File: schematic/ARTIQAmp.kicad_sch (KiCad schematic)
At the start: 28 parts, among them J1 Power conneciton, J2 HD68, J3 HD68, J4 TSM-102-01-L-DV

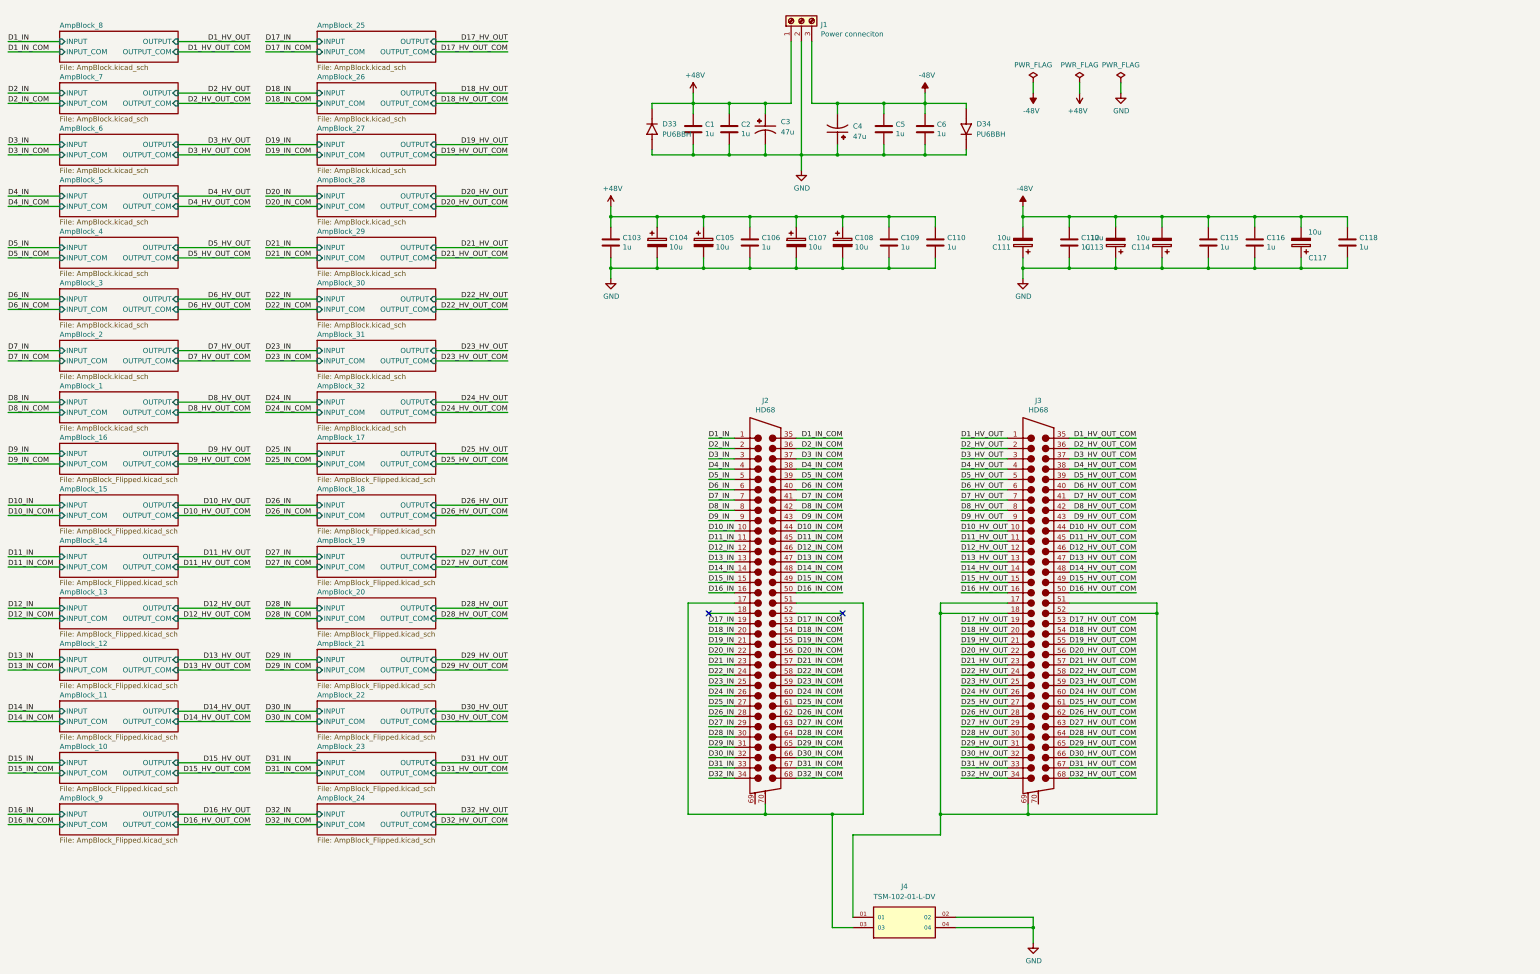
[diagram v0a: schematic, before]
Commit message: Update board design to better support enclosure with fan connect and diode connect headers. Also widen differential choke land pads and include enclosure CAD.
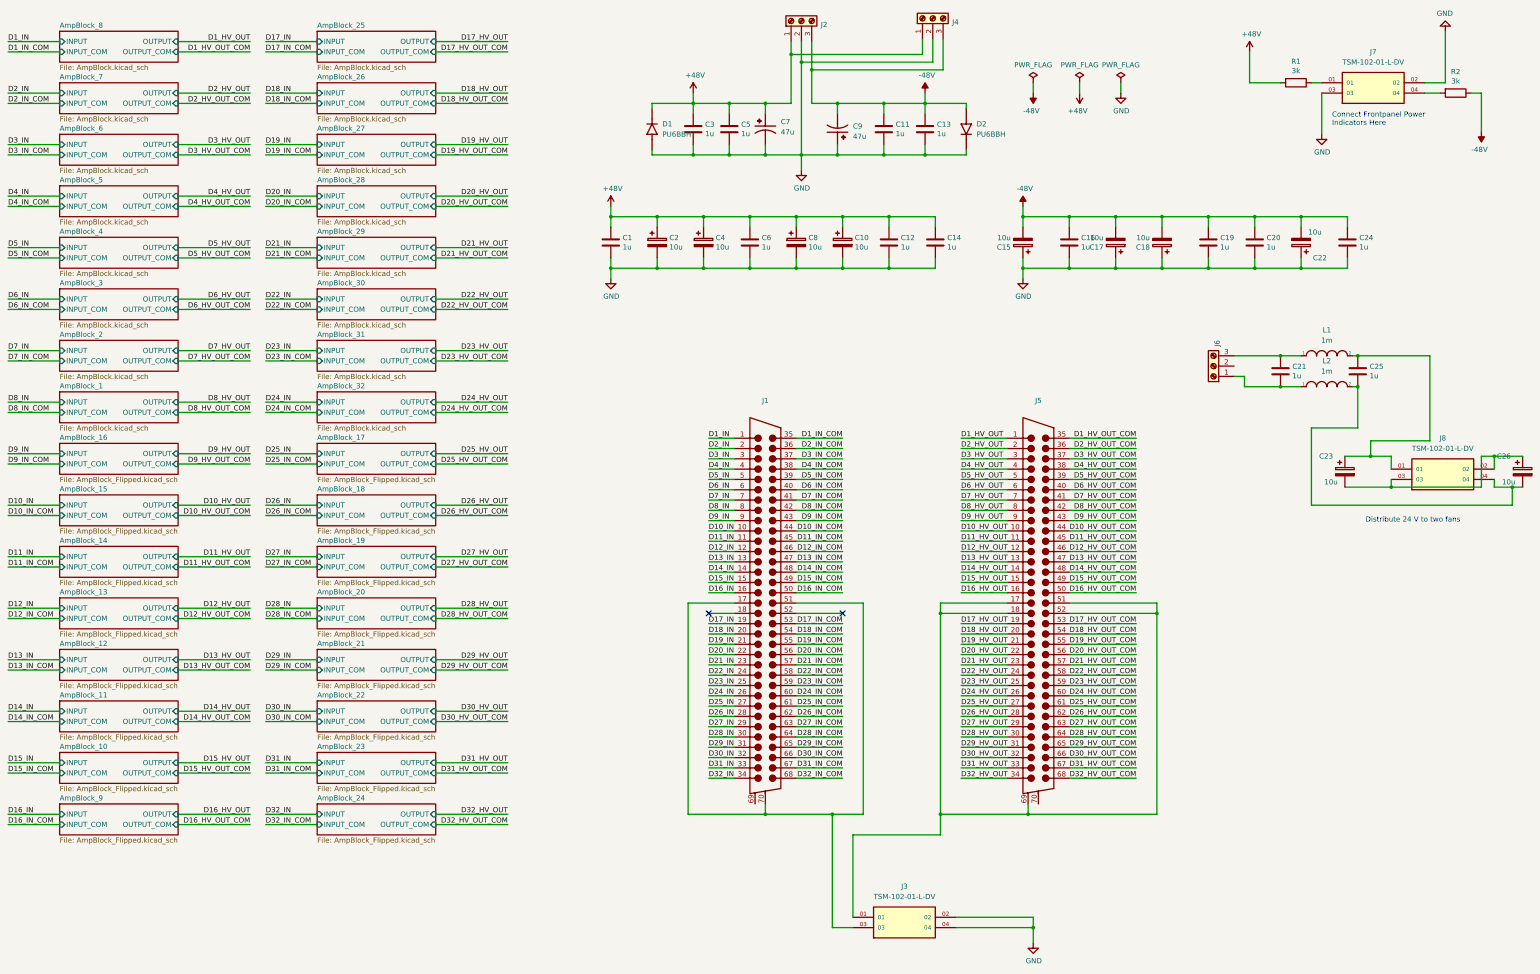
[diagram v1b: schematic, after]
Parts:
- added C21, C25: 1u, Capacitor_SMD:C_1206_3216Metric, symbol Device:C
- added C23, C26: 10u, ARTIQAmp:CAP_EEEFK1H100V, symbol Device:CP
- added J4, J6: (no value), TerminalBlock_Phoenix:TerminalBlock_Phoenix_PT-1,5-3-5.0-H_1x03_P5.00mm_Horizontal, symbol ARTIQAmp:Screw_Terminal_01x03
- added J7, J8: TSM-102-01-L-DV, SAMTEC_TSM-102-01-L-DV, symbol TSM-102-01-L-DV:TSM-102-01-L-DV
- added L1, L2: 1m, Inductor_SMD:L_1210_3225Metric, symbol pspice:INDUCTOR
- added R1, R2: 3k, Resistor_SMD:R_1206_3216Metric, symbol Device:R
- C1: renamed from C103; AVAILABILITY Y -> (none); Availability (none) -> Y; MANUFACTURER Samsung -> (none); MPN (none) -> CL31B105KCHNNNE; Manufacturer (none) -> Samsung; Manufacturer_Part_Number CL31B105KCHNNNE -> (none); Package (none) -> 1206
- C10: renamed from C108; AVAILABILITY Y -> (none); Availability (none) -> Y; MANUFACTURER United Chemi-Con -> (none); MPN (none) -> HHXD630ARA100MF80G; Manufacturer (none) -> United Chemi-Con; Manufacturer_Part_Number HHXD630ARA100MF80G -> (none); Package (none) -> Radial, Can - SMD
- C11: renamed from C5; AVAILABILITY Y -> (none); Availability (none) -> Y; MANUFACTURER Samsung -> (none); MPN (none) -> CL31B105KCHNNNE; Manufacturer (none) -> Samsung; Manufacturer_Part_Number CL31B105KCHNNNE -> (none); Package (none) -> 1206
- C12: renamed from C109; AVAILABILITY Y -> (none); Availability (none) -> Y; MANUFACTURER Samsung -> (none); MPN (none) -> CL31B105KCHNNNE; Manufacturer (none) -> Samsung; Manufacturer_Part_Number CL31B105KCHNNNE -> (none); Package (none) -> 1206
- C13: renamed from C6; AVAILABILITY Y -> (none); Availability (none) -> Y; MANUFACTURER Samsung -> (none); MPN (none) -> CL31B105KCHNNNE; Manufacturer (none) -> Samsung; Manufacturer_Part_Number CL31B105KCHNNNE -> (none); Package (none) -> 1206
- C14: renamed from C110; AVAILABILITY Y -> (none); Availability (none) -> Y; MANUFACTURER Samsung -> (none); MPN (none) -> CL31B105KCHNNNE; Manufacturer (none) -> Samsung; Manufacturer_Part_Number CL31B105KCHNNNE -> (none); Package (none) -> 1206
- C15: renamed from C111; AVAILABILITY Y -> (none); Availability (none) -> Y; MANUFACTURER United Chemi-Con -> (none); MPN (none) -> HHXD630ARA100MF80G; Manufacturer (none) -> United Chemi-Con; Manufacturer_Part_Number HHXD630ARA100MF80G -> (none); Package (none) -> Radial, Can - SMD; Type (none) -> SMT
- C16: renamed from C112; AVAILABILITY Y -> (none); Availability (none) -> Y; MANUFACTURER Samsung -> (none); MPN (none) -> CL31B105KCHNNNE; Manufacturer (none) -> Samsung; Manufacturer_Part_Number CL31B105KCHNNNE -> (none); Package (none) -> 1206
- C17: renamed from C113; AVAILABILITY Y -> (none); Availability (none) -> Y; MANUFACTURER United Chemi-Con -> (none); MPN (none) -> HHXD630ARA100MF80G; Manufacturer (none) -> United Chemi-Con; Manufacturer_Part_Number HHXD630ARA100MF80G -> (none); Package (none) -> Radial, Can - SMD
- C18: renamed from C114; AVAILABILITY Y -> (none); Availability (none) -> Y; MANUFACTURER United Chemi-Con -> (none); MPN (none) -> HHXD630ARA100MF80G; Manufacturer (none) -> United Chemi-Con; Manufacturer_Part_Number HHXD630ARA100MF80G -> (none); Package (none) -> Radial, Can - SMD
- C19: renamed from C115; AVAILABILITY Y -> (none); Availability (none) -> Y; MANUFACTURER Samsung -> (none); MPN (none) -> CL31B105KCHNNNE; Manufacturer (none) -> Samsung; Manufacturer_Part_Number CL31B105KCHNNNE -> (none); Package (none) -> 1206
- C2: renamed from C104; AVAILABILITY Y -> (none); Availability (none) -> Y; MANUFACTURER United Chemi-Con -> (none); MPN (none) -> HHXD630ARA100MF80G; Manufacturer (none) -> United Chemi-Con; Manufacturer_Part_Number HHXD630ARA100MF80G -> (none); Package (none) -> Radial, Can - SMD
- C20: renamed from C116; AVAILABILITY Y -> (none); Availability (none) -> Y; MANUFACTURER Samsung -> (none); MPN (none) -> CL31B105KCHNNNE; Manufacturer (none) -> Samsung; Manufacturer_Part_Number CL31B105KCHNNNE -> (none); Package (none) -> 1206
- C22: renamed from C117; AVAILABILITY Y -> (none); Availability (none) -> Y; MANUFACTURER United Chemi-Con -> (none); MPN (none) -> HHXD630ARA100MF80G; Manufacturer (none) -> United Chemi-Con; Manufacturer_Part_Number HHXD630ARA100MF80G -> (none); Package (none) -> Radial, Can - SMD
- C24: renamed from C118; AVAILABILITY Y -> (none); Availability (none) -> Y; MANUFACTURER Samsung -> (none); MPN (none) -> CL31B105KCHNNNE; Manufacturer (none) -> Samsung; Manufacturer_Part_Number CL31B105KCHNNNE -> (none); Package (none) -> 1206
- C3: renamed from C1; AVAILABILITY Y -> (none); Availability (none) -> Y; MANUFACTURER Samsung -> (none); MPN (none) -> CL31B105KCHNNNE; Manufacturer (none) -> Samsung; Manufacturer_Part_Number CL31B105KCHNNNE -> (none); Package (none) -> 1206
- C4: renamed from C105; AVAILABILITY Y -> (none); Availability (none) -> Y; MANUFACTURER United Chemi-Con -> (none); MPN (none) -> HHXD630ARA100MF80G; Manufacturer (none) -> United Chemi-Con; Manufacturer_Part_Number HHXD630ARA100MF80G -> (none); Package (none) -> Radial, Can - SMD
- C5: renamed from C2; AVAILABILITY Y -> (none); Availability (none) -> Y; MANUFACTURER Samsung -> (none); MPN (none) -> CL31B105KCHNNNE; Manufacturer (none) -> Samsung; Manufacturer_Part_Number CL31B105KCHNNNE -> (none); Package (none) -> 1206
- C6: renamed from C106; AVAILABILITY Y -> (none); Availability (none) -> Y; MANUFACTURER Samsung -> (none); MPN (none) -> CL31B105KCHNNNE; Manufacturer (none) -> Samsung; Manufacturer_Part_Number CL31B105KCHNNNE -> (none); Package (none) -> 1206
- C7: renamed from C3; AVAILABILITY Y -> (none); Availability (none) -> Y; MANUFACTURER Panasonic -> (none); MPN (none) -> EEE-FK2A470AV; Manufacturer (none) -> Panasonic; Manufacturer_Part_Number EEE-FK2A470AV -> (none); Type (none) -> SMT
- C8: renamed from C107; AVAILABILITY Y -> (none); Availability (none) -> Y; MANUFACTURER United Chemi-Con -> (none); MPN (none) -> HHXD630ARA100MF80G; Manufacturer (none) -> United Chemi-Con; Manufacturer_Part_Number HHXD630ARA100MF80G -> (none); Package (none) -> Radial, Can - SMD; Type (none) -> SMT
- C9: renamed from C4; AVAILABILITY Y -> (none); Availability (none) -> Y; MANUFACTURER Panasonic -> (none); MPN (none) -> EEE-FK2A470AV; Manufacturer (none) -> Panasonic; Manufacturer_Part_Number EEE-FK2A470AV -> (none); Type (none) -> SMT
- D1: renamed from D33; AVAILABILITY Y -> (none); Availability (none) -> Y; MANUFACTURER Taiwan Semiconductor -> (none); MPN (none) -> PU6BBH; Manufacturer (none) -> Taiwan Semiconductor; Manufacturer_Part_Number PU6BBH -> (none); Package (none) -> DO-214AA, SMB; Type (none) -> SMT
- D2: renamed from D34; AVAILABILITY Y -> (none); Availability (none) -> Y; MANUFACTURER Taiwan Semiconductor -> (none); MPN (none) -> PU6BBH; Manufacturer (none) -> Taiwan Semiconductor; Manufacturer_Part_Number PU6BBH -> (none)
- J1: renamed from J2; value HD68 -> (none); AVAILABILITY Y -> (none); Availability (none) -> Y; MANUFACTURER TE Connectivity AMP Connectors -> (none); MPN (none) -> 5787082-7; Manufacturer (none) -> TE Connectivity AMP Connectors; Manufacturer_Part_Number 5787082-7 -> (none); Type (none) -> Through
- J2: renamed from J1; value Power conneciton -> (none); AVAILABILITY Y -> (none); Availability (none) -> Y; MANUFACTURER Phoenix Contact -> (none); MPN (none) -> 1935174; Manufacturer (none) -> Phoenix Contact; Manufacturer_Part_Number 1935174 -> (none); Type (none) -> Through
- J3: renamed from J4; AVAILABILITY Y -> (none); Availability (none) -> Y; MANUFACTURER Samtec Inc. -> (none); MPN (none) -> TSM-102-01-L-DV; Manufacturer (none) -> Samtec Inc.; Manufacturer_Part_Number TSM-102-01-L-DV -> (none); Type (none) -> SMT
- J5: renamed from J3; value HD68 -> (none); AVAILABILITY Y -> (none); Availability (none) -> Y; MANUFACTURER TE Connectivity AMP Connectors -> (none); MPN (none) -> 5787082-7; Manufacturer (none) -> TE Connectivity AMP Connectors; Manufacturer_Part_Number 5787082-7 -> (none)
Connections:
- net +48V: now also J4.1 (Pin_1), R1.2
- net -48V: now also J4.3 (Pin_3), R2.1
- net GND: now also J4.2 (Pin_2), J7.02, J7.03
- new net: J7.01, R1.1
- new net: J7.04, R2.2
- new net: C23.2, C26.1, J8.02, J8.03
- new net: C25.2, C26.2, J8.04, L2.2
- new net: C21.1, J6.3 (Pin_3), L1.1
- new net: C23.1, C25.1, J8.01, L1.2
- new net: C21.2, J6.1 (Pin_1), L2.1
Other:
- note added: "Connect Frontpanel Power Indicators Here"
- note added: "Distribute 24 V to two fans"
